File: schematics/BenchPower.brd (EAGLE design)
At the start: 80 x 67 mm, 28 parts, among them U1 V_REG_317SINK, X2 9090-4R

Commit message: Updates for rev 2
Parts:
- removed R10: 140, SparkFun-Passives:AXIAL-0.3
- removed R3: 100, SparkFun-Passives:AXIAL-0.3
- removed U$6: BINDINGPOST, desjardins:BINDINGPOST
- moved U$3 27.9 mm to (30.5, 13.3)
- moved LED1 13.5 mm to (30.5, 2.54)
- moved R1 12.1 mm to (20.3, 14.6)
- moved U$5 7.01 mm to (40.0, 6.35)
- moved R6 5.08 mm to (53.3, 32.4)
- moved R7 5.08 mm to (65.4, 32.4)
- moved R4 5.08 mm to (71.8, 31.1)
- moved R5 5.08 mm to (74.3, 31.1)
- moved R8 5.08 mm to (57.8, 31.1)
- moved R9 5.08 mm to (69.2, 31.1)
- moved U5 5.08 mm to (53.3, 28.6)
- moved U6 5.08 mm to (65.4, 28.6)
- moved U$2 4.45 mm to (78.1, 22.2)
- moved S2 1.91 mm to (6.35, 24.1)
- moved U$4 1.87 mm to (40.0, 31.1), turned to 0 degrees
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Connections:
- net 12VHDRSW: no longer R10.P$2
- net 12VHDRTAP: no longer R10.P$1, R3.P$2
- net GND: no longer R3.P$1, U$6.P$1
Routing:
- net LCD_RS: track 15.2 -> 86.0 mm
- net LCD_EN: track 17.4 -> 79.2 mm
- net LCD_DB4: track 27.5 -> 73.8 mm
- net LCD_DB5: track 27.5 -> 69.4 mm
- net LCD_DB6: track 27.5 -> 65.1 mm
- net LCD_DB7: track 27.5 -> 61.1 mm
- net 12VHDRSW: track 155.6 -> 126.0 mm
- net LCD_CONTRAST: track 66.2 -> 38.6 mm
- net 5VARDU: track 98.2 -> 75.4 mm
- net 12VHDR: track 108.0 -> 124.7 mm, vias 1 -> 0
- net N$1: track 3.44 -> 14.2 mm
- net AMPS12VREG: track 61.5 -> 52.7 mm
- net 12VREG: track 39.0 -> 45.3 mm
- net 12VHDRTAP: track 6.35 -> 0.00 mm
- net 5VHDR: track 65.2 -> 69.6 mm
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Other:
- board text added: "gnd"
- board text added: "v2.0 (c) 2014"
- board text removed: "v1.0 (c) 2014"

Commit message: Add code, and update to rev to of hardware
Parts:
- added JP2, JP3: M02PTH, SparkFun-Connectors:1X02
- added R10: 140, SparkFun-Passives:AXIAL-0.3
- added R3: 100, SparkFun-Passives:AXIAL-0.3
- moved U$3 48.7 mm to (78.7, 19.7), turned to 90 degrees
- moved LED1 20.1 mm to (10.8, 6.35), turned to 180 degrees
- moved JP4 19.2 mm to (48.6, 4.45)
- moved JP1 10.2 mm to (2.86, 4.45)
- moved R1 6.35 mm to (15.2, 18.4), turned to 270 degrees
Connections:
- net 12VHDRSW: now also R10.P$2
- net 12VHDRTAP: now also R10.P$1, R3.P$2
- net GND: now also JP2.1, JP2.2, JP3.1, JP3.2, R3.P$1
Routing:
- net 12VHDRSW: track 126.0 -> 118.6 mm
- net N$1: track 14.2 -> 9.57 mm
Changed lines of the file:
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@@
 <element name="U$2" library="ChrisD" package="ARDUINO_PRO_MICRO" value="ARDUINO_PRO_MICRO" x="78.105" y="22.225" rot="R90"/>
 <element name="U1" library="SparkFun-PowerIC" package="TO220-ADJ" value="V_REG_317SINK" x="77.47" y="61.595" rot="R90"/>
-<element name="R1" library="SparkFun-Passives" package="AXIAL-0.3" value="1000" x="20.32" y="14.605"/>
+<element name="R1" library="SparkFun-Passives" package="AXIAL-0.3" value="1000" x="15.24" y="18.415" rot="R270"/>
 <element name="R2" library="SparkFun-Passives" package="AXIAL-0.3" value="240" x="73.025" y="55.245" rot="R270"/>
-<element name="U$3" library="desjardins" package="LOGO" value="" x="30.48" y="13.335"/>
+<element name="U$3" library="desjardins" package="LOGO" value="" x="78.74" y="19.685" rot="R90"/>
 <element name="U$4" library="desjardins" package="DT162C" value="16X2LCDDT162C" x="40.01" y="31.135"/>
 <element name="RV3" library="desjardins" package="POTRK09K111" value="" x="72.39" y="2.54"/>
-<element name="LED1" library="adafruit" package="LED3MM" value="" x="30.48" y="2.54"/>
+<element name="LED1" library="adafruit" package="LED3MM" value="" x="10.795" y="6.35" rot="R180"/>
 <element name="R6" library="SparkFun-Resistors" package="1206" value="" x="53.34" y="32.385" rot="R180"/>
 <element name="R7" library="SparkFun-Resistors" package="1206" value="" x="65.405" y="32.385" rot="R180"/>
@@
 <element name="R5" library="SparkFun-Passives" package="AXIAL-0.3" value="140" x="74.295" y="31.115" rot="R90"/>
 <element name="RV1" library="desjardins" package="3266W" value="" x="7.62" y="9.525" rot="R180"/>
-<element name="JP1" library="SparkFun-Connectors" package="1X02" value="M02PTH" x="10.795" y="10.795"/>
-<element name="JP4" library="SparkFun-Connectors" package="1X02" value="M02PTH" x="66.675" y="10.795"/>
+<element name="JP1" library="SparkFun-Connectors" package="1X02" value="M02PTH" x="2.8575" y="4.445"/>
+<element name="JP4" library="SparkFun-Connectors" package="1X02" value="M02PTH" x="48.5775" y="4.445"/>
 <element name="U5" library="SparkFun-AnalogIC" package="SOT23-5" value="" x="53.34" y="28.575" rot="R90"/>
 <element name="U6" library="SparkFun-AnalogIC" package="SOT23-5" value="" x="65.405" y="28.575" rot="R90"/>
@@
 <element name="R9" library="SparkFun-Passives" package="AXIAL-0.3" value="gain" x="69.215" y="31.115" rot="R270"/>
 <element name="S2" library="desjardins" package="EG1213" value="EG1213" x="6.35" y="24.13" rot="R270"/>
+<element name="JP2" library="SparkFun-Connectors" package="1X02" value="M02PTH" x="28.8925" y="4.445"/>
+<element name="JP3" library="SparkFun-Connectors" package="1X02" value="M02PTH" x="74.93" y="11.43"/>
+<element name="R3" library="SparkFun-Passives" package="AXIAL-0.3" value="100" x="0.635" y="-2.54"/>
+<element name="R10" library="SparkFun-Passives" package="AXIAL-0.3" value="140" x="0.635" y="-5.715"/>
 </elements>
 <signals>
@@
 <contactref element="U$4" pad="P$16"/>
 <contactref element="RV1" pad="P$1"/>
-<contactref element="JP1" pad="1"/>
-<contactref element="JP1" pad="2"/>
-<contactref element="JP4" pad="1"/>
-<contactref element="JP4" pad="2"/>
 <contactref element="U5" pad="2"/>
 <contactref element="U6" pad="2"/>
 <contactref element="R8" pad="P$1"/>
 <contactref element="R9" pad="P$1"/>
+<contactref element="JP1" pad="2"/>
+<contactref element="JP1" pad="1"/>
+<contactref element="JP2" pad="2"/>
+<contactref element="JP2" pad="1"/>
+<contactref element="JP3" pad="2"/>
+<contactref element="JP3" pad="1"/>
+<contactref element="JP4" pad="2"/>
+<contactref element="JP4" pad="1"/>
+<contactref element="R3" pad="P$1"/>
+<wire x1="54.56" y1="50.38" x2="54.56" y2="55.88" width="0" layer="19" extent="1-1"/>
+<wire x1="50.36" y1="50.38" x2="54.56" y2="50.38" width="0" layer="19" extent="1-1"/>
+<wire x1="46.16" y1="50.38" x2="50.36" y2="50.38" width="0" layer="19" extent="1-1"/>
+<wire x1="46.11" y1="47.135" x2="46.16" y2="50.38" width="0" layer="19" extent="1-1"/>
+<wire x1="41.96" y1="50.38" x2="46.16" y2="50.38" width="0" layer="19" extent="1-1"/>
+<wire x1="37.76" y1="50.38" x2="41.96" y2="50.38" width="0" layer="19" extent="1-1"/>
+<wire x1="46.16" y1="55.88" x2="46.16" y2="50.38" width="0" layer="19" extent="1-1"/>
+<wire x1="37.76" y1="55.88" x2="37.76" y2="50.38" width="0" layer="19" extent="1-1"/>
+<wire x1="41.275" y1="38.735" x2="46.11" y2="47.135" width="0" layer="19" extent="1-1"/>
+<wire x1="57.785" y1="34.925" x2="54.56" y2="50.38" width="0" layer="19" extent="1-1"/>
+<wire x1="54.6401" y1="28.575" x2="57.785" y2="34.925" width="0" layer="19" extent="1-1"/>
+<wire x1="46.355" y1="23.495" x2="54.6401" y2="28.575" width="0" layer="19" extent="1-1"/>
+<wire x1="66.7051" y1="28.575" x2="57.785" y2="34.925" width="0" layer="19" extent="1-1"/>
+<wire x1="69.215" y1="34.925" x2="66.7051" y2="28.575" width="0" layer="19" extent="1-1"/>
+<wire x1="71.755" y1="34.925" x2="69.215" y2="34.925" width="0" layer="19" extent="1-1"/>
+<wire x1="40.005" y1="6.35" x2="46.355" y2="23.495" width="0" layer="19" extent="1-1"/>
+<wire x1="48.5775" y1="4.445" x2="40.005" y2="6.35" width="0" layer="19" extent="1-1"/>
+<wire x1="51.1175" y1="4.445" x2="48.5775" y2="4.445" width="0" layer="19" extent="1-1"/>
+<wire x1="31.4325" y1="4.445" x2="40.005" y2="6.35" width="0" layer="19" extent="1-1"/>
+<wire x1="28.8925" y1="4.445" x2="31.4325" y2="4.445" width="0" layer="19" extent="1-1"/>
+<wire x1="74.93" y1="11.43" x2="66.7051" y2="28.575" width="0" layer="19" extent="1-1"/>
+<wire x1="77.47" y1="11.43" x2="74.93" y2="11.43" width="0" layer="19" extent="1-1"/>
+<wire x1="74.89" y1="2.54" x2="74.93" y2="11.43" width="0" layer="19" extent="1-1"/>
+<wire x1="9.525" y1="6.35" x2="28.8925" y2="4.445" width="0" layer="19" extent="1-1"/>
+<wire x1="7.62" y1="9.525" x2="9.525" y2="6.35" width="0" layer="19" extent="1-1"/>
+<wire x1="5.3975" y1="4.445" x2="9.525" y2="6.35" width="0" layer="19" extent="1-1"/>
+<wire x1="2.8575" y1="4.445" x2="5.3975" y2="4.445" width="0" layer="19" extent="1-1"/>
+<wire x1="-3.175" y1="-2.54" x2="2.8575" y2="4.445" width="0" layer="19" extent="1-1"/>
+<wire x1="18.17" y1="47.135" x2="37.76" y2="50.38" width="0" layer="19" extent="1-1"/>
+<wire x1="15.24" y1="53.975" x2="18.17" y2="47.135" width="0" layer="19" extent="1-1"/>
+<wire x1="10.16" y1="53.975" x2="15.24" y2="53.975" width="0" layer="19" extent="1-1"/>
+<wire x1="8.01" y1="47.135" x2="10.16" y2="53.975" width="0" layer="19" extent="1-1"/>
 </signal>
 <signal name="5VSB">
@@
 <contactref element="R1" pad="P$2"/>
 <contactref element="LED1" pad="A"/>
-<wire x1="24.13" y1="14.605" x2="29.21" y2="9.525" width="0.4064" layer="1"/>
-<wire x1="29.21" y1="9.525" x2="29.21" y2="2.54" width="0.4064" layer="1"/>
+<wire x1="15.24" y1="14.605" x2="12.065" y2="11.43" width="0.4064" layer="1"/>
+<wire x1="12.065" y1="11.43" x2="12.065" y2="6.35" width="0.4064" layer="1"/>
 </signal>
 <signal name="PWR_OK">
@@
 <signal name="12VHDRTAP">
 <contactref element="U$2" pad="P25"/>
+<contactref element="R3" pad="P$2"/>
+<contactref element="R10" pad="P$1"/>
+<wire x1="4.445" y1="-2.54" x2="56.515" y2="38.735" width="0" layer="19" extent="1-1"/>
+<wire x1="-3.175" y1="-5.715" x2="4.445" y2="-2.54" width="0" layer="19" extent="1-1"/>
 </signal>
 <signal name="12VHDRSW">
@@
 <contactref element="R6" pad="1"/>
 <wire x1="54.6401" y1="32.2851" x2="54.74" y2="32.385" width="0.6096" layer="1"/>
-<wire x1="53.975" y1="35.56" x2="55.245" y2="34.29" width="0.8128" layer="1"/>
-<wire x1="55.245" y1="34.29" x2="55.245" y2="32.89" width="0.8128" layer="1"/>
 <wire x1="55.245" y1="32.89" x2="54.74" y2="32.385" width="0.8128" layer="1"/>
 <wire x1="70.485" y1="45.085" x2="70.485" y2="60.96" width="0.8128" layer="1"/>
@@
 <contactref element="R1" pad="P$1"/>
 <wire x1="15.24" y1="24.13" x2="6.35" y2="24.13" width="0.8128" layer="1"/>
-<wire x1="15.24" y1="24.13" x2="15.24" y2="15.875" width="0.4064" layer="1"/>
-<wire x1="15.24" y1="15.875" x2="16.51" y2="14.605" width="0.4064" layer="1"/>
-<wire x1="15.24" y1="24.13" x2="26.67" y2="35.56" width="0.8128" layer="1"/>
-<wire x1="26.67" y1="35.56" x2="53.975" y2="35.56" width="0.8128" layer="1"/>
+<wire x1="15.24" y1="24.13" x2="27.94" y2="36.83" width="0.8128" layer="1"/>
 <wire x1="70.485" y1="45.085" x2="76.2" y2="39.37" width="0.8128" layer="1"/>
 <wire x1="76.2" y1="39.37" x2="76.2" y2="38.1" width="0.8128" layer="1"/>
 <wire x1="76.2" y1="38.1" x2="74.93" y2="36.83" width="0.8128" layer="1"/>
-<wire x1="74.93" y1="36.83" x2="55.245" y2="36.83" width="0.8128" layer="1"/>
-<wire x1="55.245" y1="36.83" x2="53.975" y2="35.56" width="0.8128" layer="1"/>
+<wire x1="15.24" y1="22.225" x2="15.24" y2="24.13" width="0.4064" layer="1"/>
+<wire x1="55.245" y1="32.89" x2="55.245" y2="36.83" width="0.8128" layer="1"/>
+<wire x1="55.245" y1="36.83" x2="74.93" y2="36.83" width="0.8128" layer="1"/>
+<wire x1="27.94" y1="36.83" x2="55.245" y2="36.83" width="0.8128" layer="1"/>
+<contactref element="R10" pad="P$2"/>
+<wire x1="4.445" y1="-5.715" x2="6.35" y2="24.13" width="0" layer="19" extent="1-1"/>
 </signal>
 </signals>

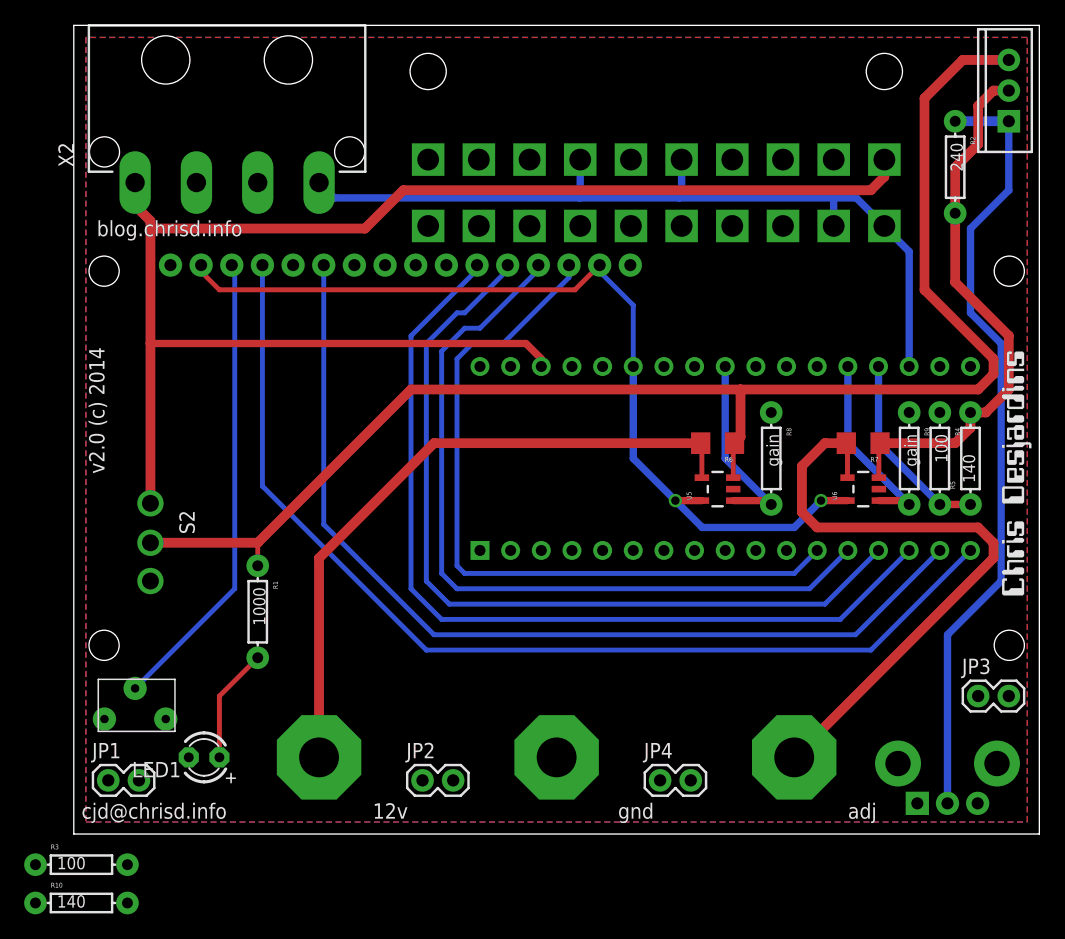
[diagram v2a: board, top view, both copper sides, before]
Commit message: Adding updates for v2.0 and source code for arduino
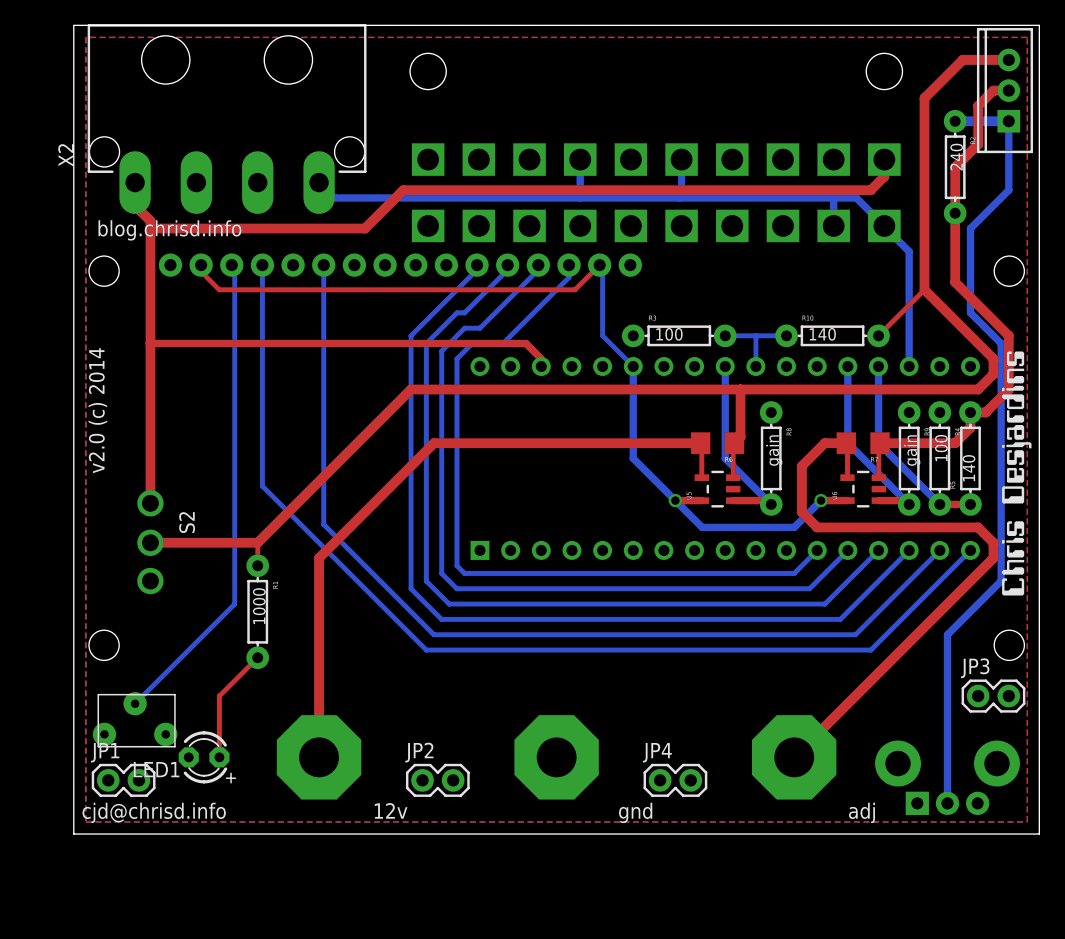
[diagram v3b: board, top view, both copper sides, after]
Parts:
- moved R10 78.0 mm to (62.9, 41.3)
- moved R3 66.1 mm to (50.2, 41.3)
- moved RV1 1.27 mm to (7.62, 8.26)
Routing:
- net 12VHDRTAP: track 0.00 -> 7.62 mm
- net 12VHDRSW: track 118.6 -> 124.0 mm
- net LCD_CONTRAST: track 38.6 -> 39.9 mm
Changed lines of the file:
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@@
 <element name="R4" library="SparkFun-Passives" package="AXIAL-0.3" value="100" x="71.755" y="31.115" rot="R270"/>
 <element name="R5" library="SparkFun-Passives" package="AXIAL-0.3" value="140" x="74.295" y="31.115" rot="R90"/>
-<element name="RV1" library="desjardins" package="3266W" value="" x="7.62" y="9.525" rot="R180"/>
+<element name="RV1" library="desjardins" package="3266W" value="" x="7.62" y="8.255" rot="R180"/>
 <element name="JP1" library="SparkFun-Connectors" package="1X02" value="M02PTH" x="2.8575" y="4.445"/>
 <element name="JP4" library="SparkFun-Connectors" package="1X02" value="M02PTH" x="48.5775" y="4.445"/>
@@
 <element name="JP2" library="SparkFun-Connectors" package="1X02" value="M02PTH" x="28.8925" y="4.445"/>
 <element name="JP3" library="SparkFun-Connectors" package="1X02" value="M02PTH" x="74.93" y="11.43"/>
-<element name="R3" library="SparkFun-Passives" package="AXIAL-0.3" value="100" x="0.635" y="-2.54"/>
-<element name="R10" library="SparkFun-Passives" package="AXIAL-0.3" value="140" x="0.635" y="-5.715"/>
+<element name="R3" library="SparkFun-Passives" package="AXIAL-0.3" value="100" x="50.165" y="41.275"/>
+<element name="R10" library="SparkFun-Passives" package="AXIAL-0.3" value="140" x="62.865" y="41.275"/>
 </elements>
 <signals>
@@
 <contactref element="JP4" pad="1"/>
 <contactref element="R3" pad="P$1"/>
-<wire x1="54.56" y1="50.38" x2="54.56" y2="55.88" width="0" layer="19" extent="1-1"/>
-<wire x1="50.36" y1="50.38" x2="54.56" y2="50.38" width="0" layer="19" extent="1-1"/>
-<wire x1="46.16" y1="50.38" x2="50.36" y2="50.38" width="0" layer="19" extent="1-1"/>
-<wire x1="46.11" y1="47.135" x2="46.16" y2="50.38" width="0" layer="19" extent="1-1"/>
-<wire x1="41.96" y1="50.38" x2="46.16" y2="50.38" width="0" layer="19" extent="1-1"/>
-<wire x1="37.76" y1="50.38" x2="41.96" y2="50.38" width="0" layer="19" extent="1-1"/>
-<wire x1="46.16" y1="55.88" x2="46.16" y2="50.38" width="0" layer="19" extent="1-1"/>
-<wire x1="37.76" y1="55.88" x2="37.76" y2="50.38" width="0" layer="19" extent="1-1"/>
-<wire x1="41.275" y1="38.735" x2="46.11" y2="47.135" width="0" layer="19" extent="1-1"/>
-<wire x1="57.785" y1="34.925" x2="54.56" y2="50.38" width="0" layer="19" extent="1-1"/>
-<wire x1="54.6401" y1="28.575" x2="57.785" y2="34.925" width="0" layer="19" extent="1-1"/>
-<wire x1="46.355" y1="23.495" x2="54.6401" y2="28.575" width="0" layer="19" extent="1-1"/>
-<wire x1="66.7051" y1="28.575" x2="57.785" y2="34.925" width="0" layer="19" extent="1-1"/>
-<wire x1="69.215" y1="34.925" x2="66.7051" y2="28.575" width="0" layer="19" extent="1-1"/>
-<wire x1="71.755" y1="34.925" x2="69.215" y2="34.925" width="0" layer="19" extent="1-1"/>
-<wire x1="40.005" y1="6.35" x2="46.355" y2="23.495" width="0" layer="19" extent="1-1"/>
-<wire x1="48.5775" y1="4.445" x2="40.005" y2="6.35" width="0" layer="19" extent="1-1"/>
-<wire x1="51.1175" y1="4.445" x2="48.5775" y2="4.445" width="0" layer="19" extent="1-1"/>
-<wire x1="31.4325" y1="4.445" x2="40.005" y2="6.35" width="0" layer="19" extent="1-1"/>
-<wire x1="28.8925" y1="4.445" x2="31.4325" y2="4.445" width="0" layer="19" extent="1-1"/>
-<wire x1="74.93" y1="11.43" x2="66.7051" y2="28.575" width="0" layer="19" extent="1-1"/>
-<wire x1="77.47" y1="11.43" x2="74.93" y2="11.43" width="0" layer="19" extent="1-1"/>
-<wire x1="74.89" y1="2.54" x2="74.93" y2="11.43" width="0" layer="19" extent="1-1"/>
-<wire x1="9.525" y1="6.35" x2="28.8925" y2="4.445" width="0" layer="19" extent="1-1"/>
-<wire x1="7.62" y1="9.525" x2="9.525" y2="6.35" width="0" layer="19" extent="1-1"/>
-<wire x1="5.3975" y1="4.445" x2="9.525" y2="6.35" width="0" layer="19" extent="1-1"/>
-<wire x1="2.8575" y1="4.445" x2="5.3975" y2="4.445" width="0" layer="19" extent="1-1"/>
-<wire x1="-3.175" y1="-2.54" x2="2.8575" y2="4.445" width="0" layer="19" extent="1-1"/>
-<wire x1="18.17" y1="47.135" x2="37.76" y2="50.38" width="0" layer="19" extent="1-1"/>
-<wire x1="15.24" y1="53.975" x2="18.17" y2="47.135" width="0" layer="19" extent="1-1"/>
-<wire x1="10.16" y1="53.975" x2="15.24" y2="53.975" width="0" layer="19" extent="1-1"/>
-<wire x1="8.01" y1="47.135" x2="10.16" y2="53.975" width="0" layer="19" extent="1-1"/>
 </signal>
 <signal name="5VSB">
@@
 <wire x1="59.69" y1="25.4" x2="52.07" y2="25.4" width="0.6096" layer="16"/>
 <wire x1="52.07" y1="25.4" x2="49.845" y2="27.625" width="0.6096" layer="16"/>
-<wire x1="46.355" y1="38.735" x2="46.355" y2="43.815" width="0.4064" layer="16"/>
-<wire x1="46.355" y1="43.815" x2="43.815" y2="46.355" width="0.4064" layer="16"/>
-<wire x1="43.815" y1="46.355" x2="43.815" y2="46.89" width="0.4064" layer="16"/>
 <wire x1="43.815" y1="46.89" x2="43.57" y2="47.135" width="0.4064" layer="16"/>
 <wire x1="10.55" y1="47.135" x2="10.55" y2="46.6" width="0.4064" layer="1"/>
@@
 <wire x1="41.52" y1="45.085" x2="43.57" y2="47.135" width="0.4064" layer="1"/>
 <wire x1="46.355" y1="31.115" x2="49.845" y2="27.625" width="0.6096" layer="16"/>
+<wire x1="46.355" y1="38.735" x2="43.815" y2="41.275" width="0.4064" layer="16"/>
+<wire x1="43.815" y1="41.275" x2="43.815" y2="46.89" width="0.4064" layer="16"/>
 </signal>
 <signal name="12VREGTAP">
@@
 <contactref element="U$4" pad="P$3"/>
 <contactref element="RV1" pad="P$2"/>
-<wire x1="13.335" y1="20.32" x2="13.335" y2="46.89" width="0.4064" layer="16"/>
+<wire x1="13.335" y1="19.05" x2="13.335" y2="46.89" width="0.4064" layer="16"/>
 <wire x1="13.335" y1="46.89" x2="13.09" y2="47.135" width="0.4064" layer="16"/>
-<wire x1="13.335" y1="20.32" x2="5.08" y2="12.065" width="0.4064" layer="16"/>
+<wire x1="13.335" y1="19.05" x2="5.08" y2="10.795" width="0.4064" layer="16"/>
 </signal>
 <signal name="12VHDRTAP">
@@
 <contactref element="R3" pad="P$2"/>
 <contactref element="R10" pad="P$1"/>
-<wire x1="4.445" y1="-2.54" x2="56.515" y2="38.735" width="0" layer="19" extent="1-1"/>
-<wire x1="-3.175" y1="-5.715" x2="4.445" y2="-2.54" width="0" layer="19" extent="1-1"/>
+<wire x1="56.515" y1="38.735" x2="56.515" y2="41.275" width="0.4064" layer="16"/>
+<wire x1="56.515" y1="41.275" x2="53.975" y2="41.275" width="0.4064" layer="16"/>
+<wire x1="59.055" y1="41.275" x2="56.515" y2="41.275" width="0.4064" layer="16"/>
 </signal>
 <signal name="12VHDRSW">
@@
 <wire x1="27.94" y1="36.83" x2="55.245" y2="36.83" width="0.8128" layer="1"/>
 <contactref element="R10" pad="P$2"/>
-<wire x1="4.445" y1="-5.715" x2="6.35" y2="24.13" width="0" layer="19" extent="1-1"/>
+<wire x1="70.485" y1="45.085" x2="66.675" y2="41.275" width="0.4064" layer="1"/>
 </signal>
 </signals>
